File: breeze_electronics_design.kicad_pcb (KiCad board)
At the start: 2 copper layers, 104.1 x 104.1 mm, 107 parts, among them J1 SIP4, M1 MotorA, M2 MotorB, M3 MotorA, M4 MotorB, Q1 S8050, Q2 SI2302, Q3 SI2302, Q4 SI2302, Q5 SI2302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

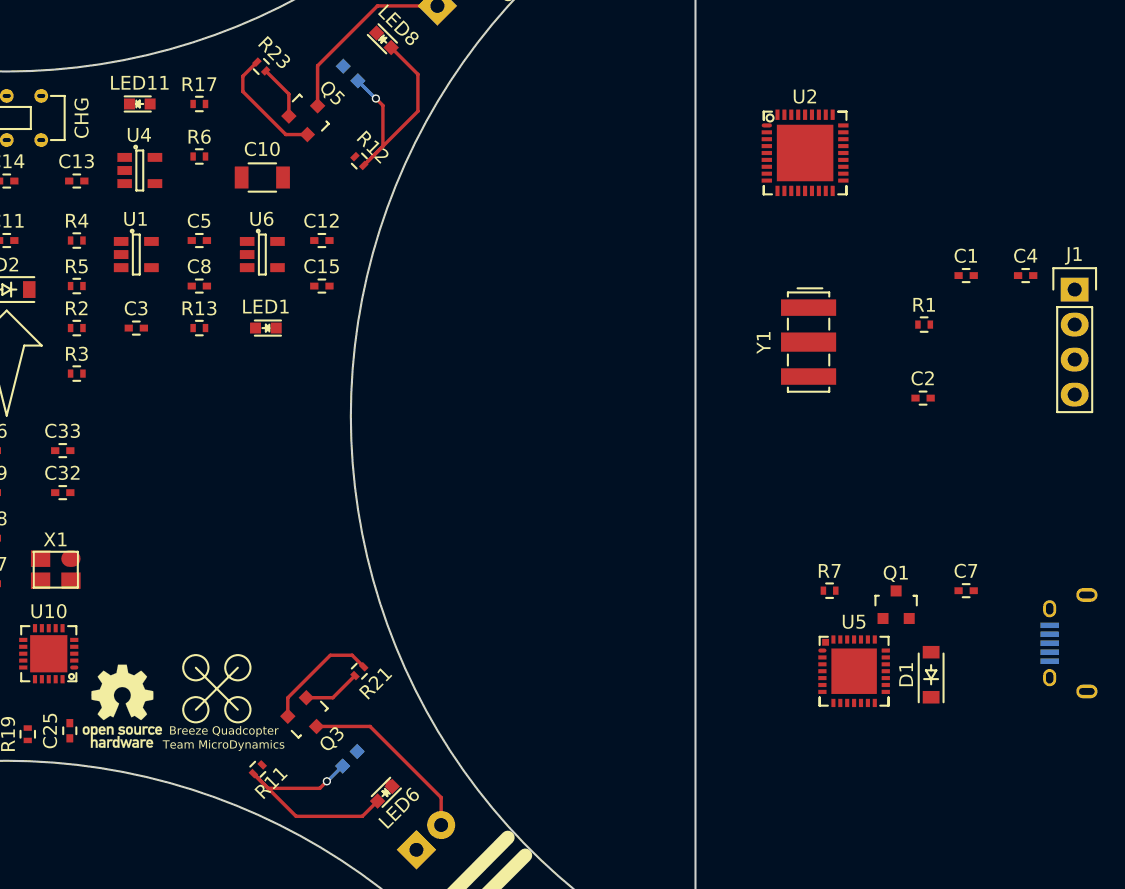
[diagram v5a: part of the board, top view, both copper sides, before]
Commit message: Relocate the footprints of MCU and Serial
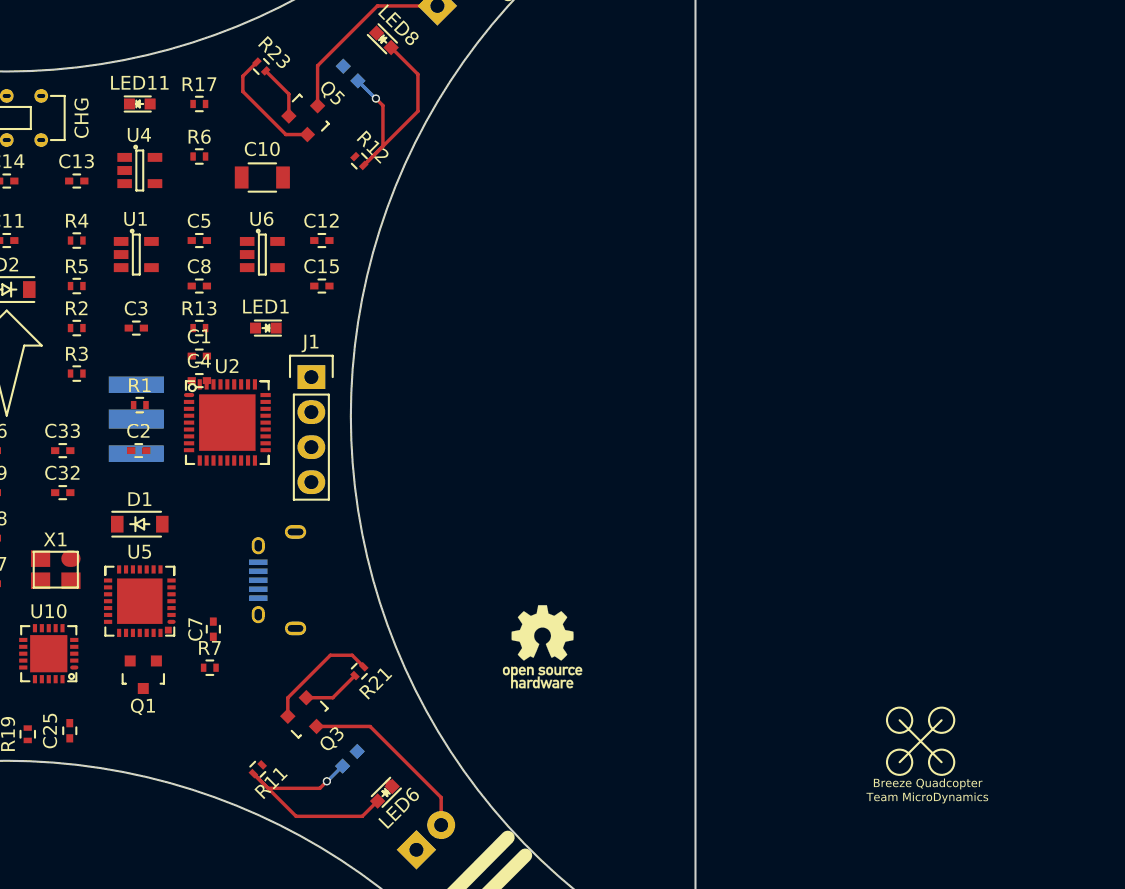
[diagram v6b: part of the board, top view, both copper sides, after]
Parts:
- Y1: moved to B.Cu
- moved C4 60.4 mm to (64.0, -52.6)
- moved D1 58.4 mm to (59.7, -42.2), turned to 0 degrees
- moved USB1 57.6 mm to (69.8, -38.1)
- moved R1 57.2 mm to (59.7, -50.8), turned to 180 degrees
- moved C2 57.0 mm to (59.6, -47.5)
- moved C1 55.9 mm to (64.0, -54.4)
- moved J1 55.7 mm to (72.1, -52.8)
- moved Q1 54.8 mm to (59.9, -31.2), turned to 180 degrees
- moved C7 54.7 mm to (65.0, -34.5), turned to 90 degrees
- moved U5 52.1 mm to (59.7, -36.6), turned to 180 degrees
- moved REF** 51.2 mm to (116.3, -26.4)
- moved Y1 49.1 mm to (59.4, -49.8)
- moved U2 46.2 mm to (66.0, -49.5)
- moved R7 45.3 mm to (64.8, -31.8), turned to 180 degrees
- moved REF*** 30.8 mm to (88.9, -33.3)

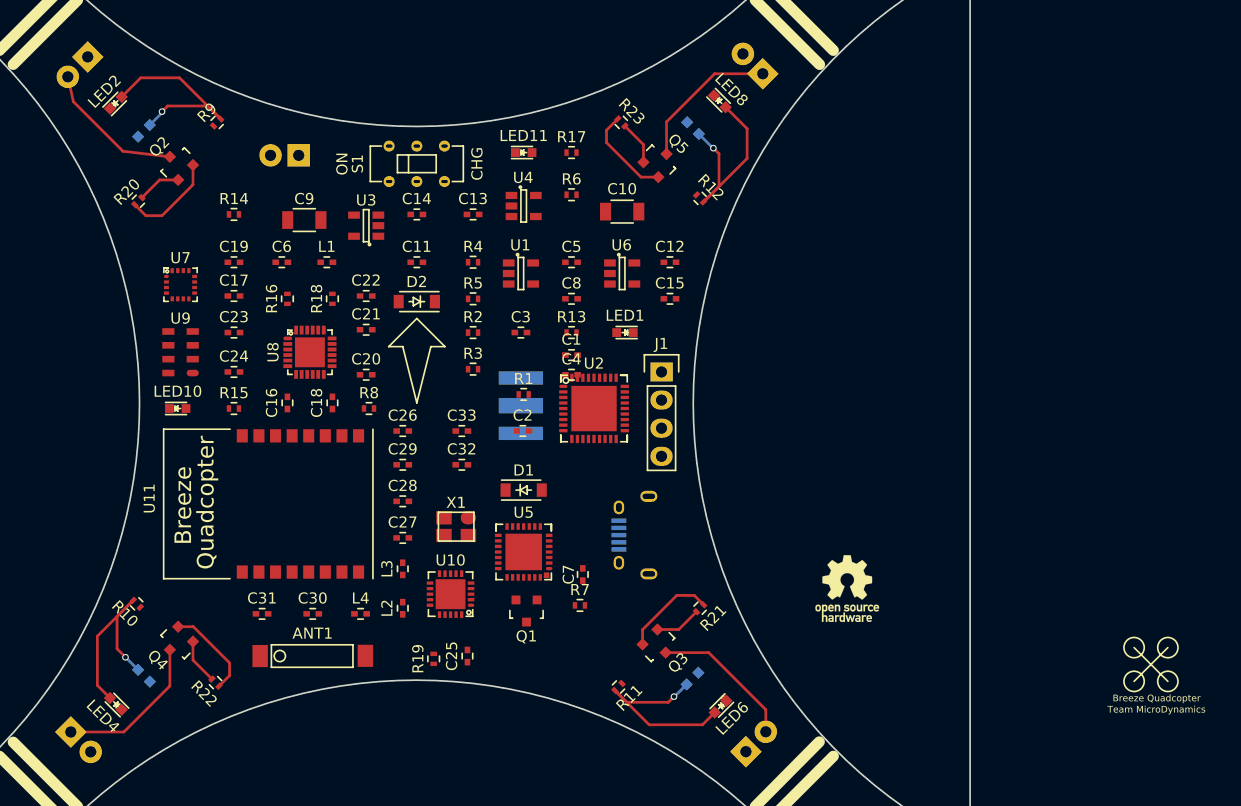
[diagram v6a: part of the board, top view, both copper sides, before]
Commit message: Make the module of Serial to the pcb's back
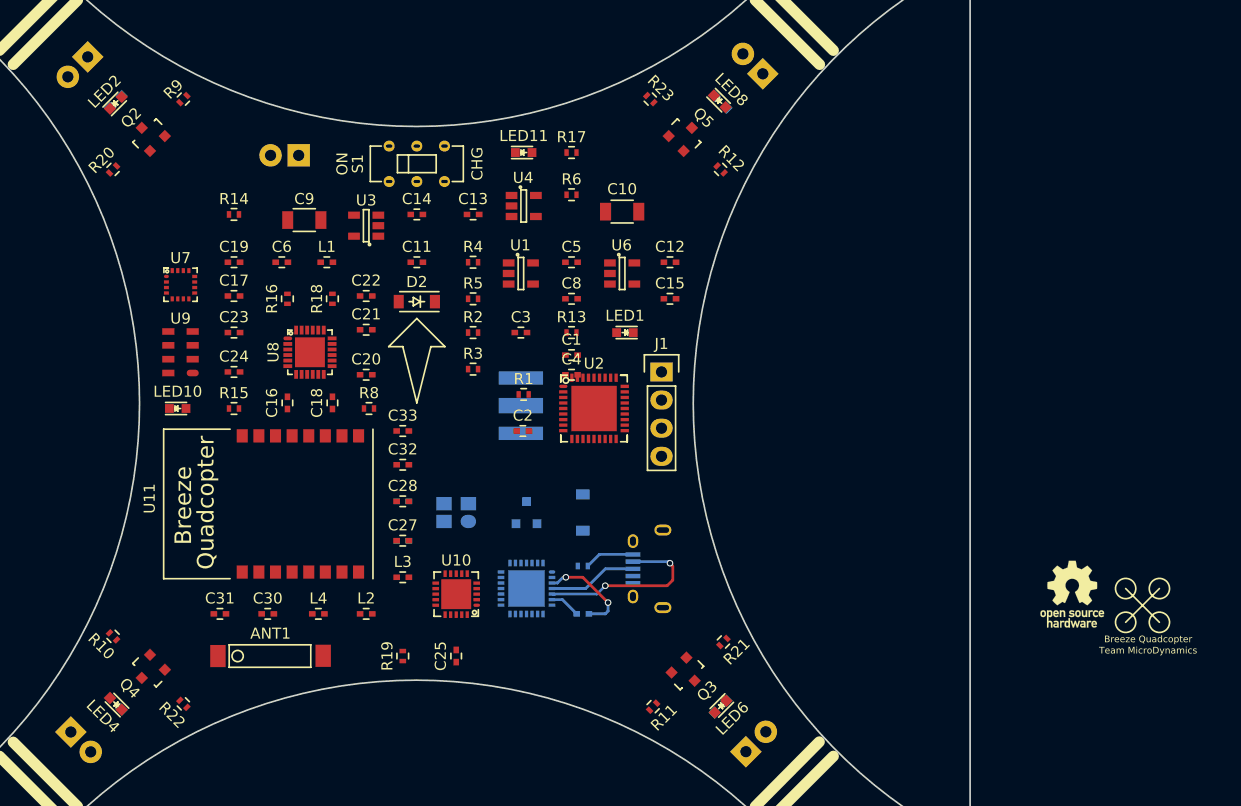
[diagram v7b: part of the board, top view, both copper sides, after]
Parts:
- C26, C29, C7, D1, Q1, R7, U5, X1: moved to B.Cu
- moved REF*** 20.3 mm to (109.2, -32.8)
- moved C26 9.91 mm to (48.8, -37.6)
- moved Q1 8.89 mm to (59.9, -40.1)
- moved D1 5.71 mm to (65.0, -40.1), turned to 270 degrees
- moved REF** 5.39 mm to (115.6, -31.8)
- moved C32 5.33 mm to (48.8, -44.5)
- moved C33 5.33 mm to (48.8, -47.5)
- moved C30 4.06 mm to (36.6, -31.0)
- moved ANT1 3.81 mm to (36.8, -27.2)
- moved C31 3.81 mm to (32.3, -31.0)
- moved L4 3.81 mm to (41.1, -31.0)
- moved R21 3.71 mm to (77.7, -28.4)
- moved R9 3.71 mm to (29.0, -77.5)
- moved R20 3.67 mm to (22.6, -71.1)
- moved LED3 3.65 mm to (22.9, -77.2)
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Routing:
- net Net-(LED2-Pad2): track 18.9 -> 0.03 mm, vias 1 -> 0
- net Net-(LED8-Pad2): track 18.5 -> 0.00 mm, vias 1 -> 0
- net Net-(LED6-Pad2): track 18.3 -> 0.00 mm, vias 1 -> 0
- net Net-(LED4-Pad2): track 18.3 -> 0.00 mm, vias 1 -> 0
- net /DN: track 0.00 -> 16.5 mm, vias 0 -> 2
- net Net-(M2-Pad1): track 13.9 -> 0.00 mm
- net Net-(M4-Pad1): track 13.4 -> 0.00 mm
- net Net-(M3-Pad2): track 13.2 -> 0.00 mm
- net Net-(M1-Pad2): track 12.9 -> 0.00 mm
- net Net-(C7-Pad1): track 0.00 -> 8.83 mm, vias 0 -> 2
- net Net-(Q2-Pad2): track 8.60 -> 0.00 mm
- net Net-(Q5-Pad2): track 8.53 -> 0.00 mm
- net Net-(Q4-Pad2): track 8.49 -> 0.00 mm
- net Net-(Q3-Pad2): track 8.47 -> 0.00 mm
- net /DP: track 0.00 -> 8.05 mm
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
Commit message: Modify the clearance from 0.2 to 0.15
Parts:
- C23, C24, U9: moved to B.Cu
- Y1: moved to F.Cu
- moved C23 5.33 mm to (28.2, -56.4)
- moved C24 5.33 mm to (28.2, -52.8)
- moved Y1 4.93 mm to (55.4, -47.0)
- moved U9 4.32 mm to (33.0, -54.6), turned to 0 degrees
- moved U2 3.31 mm to (65.8, -46.2)
- moved REF*** 2.41 mm to (108.5, -30.5)
- moved REF** 0.51 mm to (115.6, -31.2)
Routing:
- net Net-(C19-Pad1): track 0.00 -> 9.03 mm, vias 0 -> 2
- net Net-(C19-Pad2): track 0.00 -> 5.47 mm
- net Net-(C17-Pad1): track 0.00 -> 4.26 mm
